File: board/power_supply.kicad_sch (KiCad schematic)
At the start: 51 parts, among them J1 USB, J2 LiPo, J3 On/Off, J5 Temp, Q10 SI2302, Q8 SI2302, U1 LGS4056HEP, U11 FM2113, U2 TLV61048, U3 RT9069, U4 JW5026

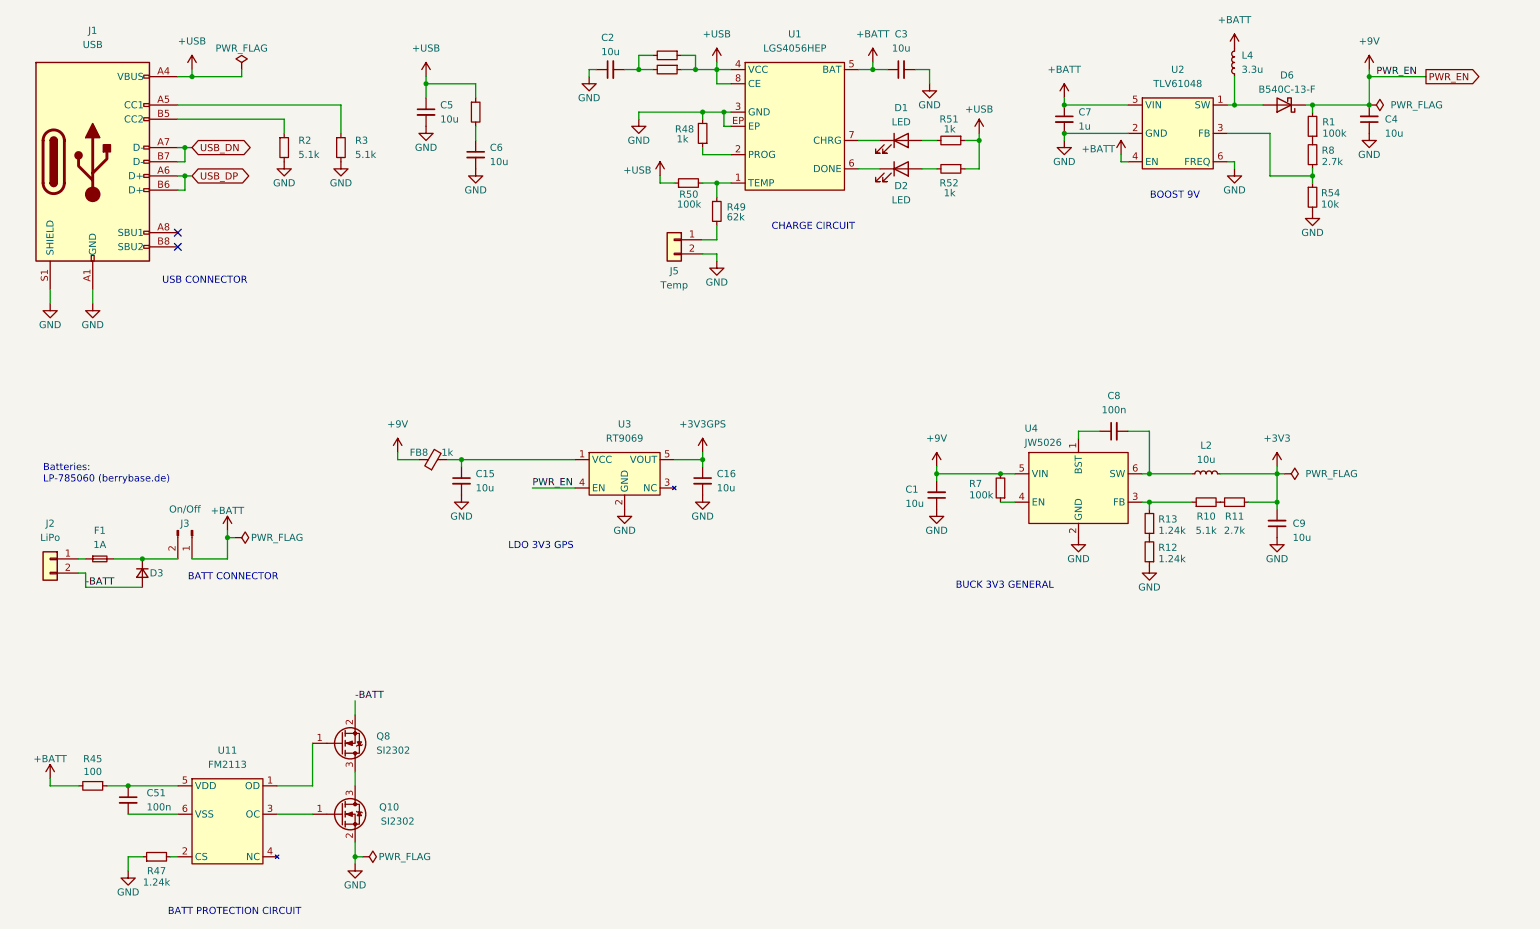
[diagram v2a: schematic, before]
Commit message: Fix errors in schematic for new board design
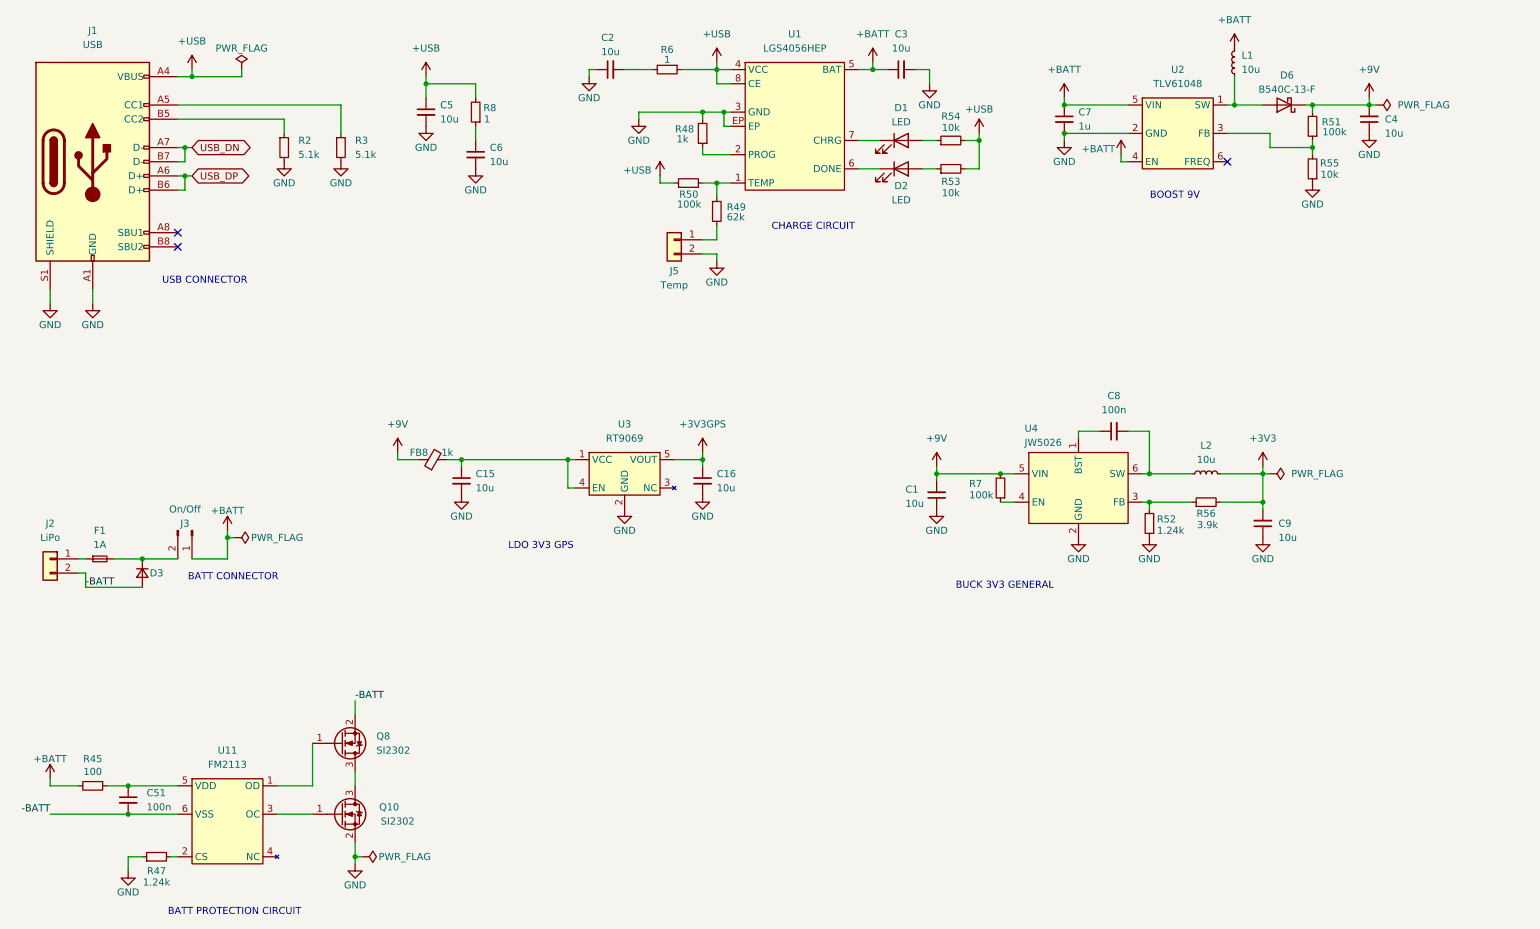
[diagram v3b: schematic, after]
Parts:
- removed L4: 3.3u, symbol Device:L_Small
- removed R1: 100k, Resistor_SMD:R_0603_1608Metric, symbol Device:R_Small
- removed R10: 5.1k, Resistor_SMD:R_0603_1608Metric, symbol Device:R_Small
- removed R11: 2.7k, Resistor_SMD:R_0603_1608Metric, symbol Device:R_Small
- removed R12, R13: 1.24k, Resistor_SMD:R_0603_1608Metric, symbol Device:R_Small
- removed R4, R5: 2, Resistor_SMD:R_0603_1608Metric, symbol Device:R_Small
- added L1: 10u, Inductor_SMD:L_6.3x6.3_H3, symbol Device:L_Small
- added R53, R55: 10k, Resistor_SMD:R_0603_1608Metric, symbol Device:R_Small
- added R56: 3.9k, Resistor_SMD:R_0603_1608Metric, symbol Device:R_Small
- C1, C15, C16, C2, C3, C4, C5, C6, C9: JLC_PN C19702 -> C962136; JLC_Price1 0.062 -> (none); JLC_Price10 0.0052 -> (none); JLC_Price100 0.0031 -> (none); JLC_Price1000 0.0029 -> (none); MPN CL10A106KP8NNNC -> CL10A106KO8NQNC
- D2: JLC_PN (none) -> C12624; JLC_Price1000 0.0036 -> (none)
- L2: footprint (none) -> Inductor_SMD:L_6.3x6.3_H3; JLC_PN (none) -> C168076
- Q10, Q8: JLC_PN (none) -> C2891732
- R49: JLC_PN (none) -> C23221
- R50, R7: JLC_PN (none) -> C25803
- R51: value 1k -> 100k; JLC_PN C21190 -> C25803; JLC_Price10 0.0005 -> (none); MPN 0603WAF1001T5E -> 0603WAF1003T5E; kicost:JLC:pricing 1: USD 0.0005; 200: USD 0.0004 -> (none)
- R52: value 1k -> 1.24k; JLC_BasicPart yes -> no; JLC_PN C21190 -> C25956; JLC_Price10 0.0005 -> (none); MPN 0603WAF1001T5E -> 0603WAF1241T5E; Manufacturer UNI-ROYAL(Uniroyal Elec) -> UNI-ROYAL(Uniroyal Elec); PCBA yes -> (none); kicost:JLC:pricing 1: USD 0.0005; 200: USD 0.0004 -> (none)
- R6: value 2 -> 1; JLC_BasicPart yes -> (none); JLC_PN C22977 -> C22936; JLC_Price10 0.0012 -> (none); MPN 0603WAF200KT5E -> 0603WAF100KT5E; PCBA yes -> (none); kicost:JLC:pricing 1: USD 0.0014; 200: USD 0.0011; 1000: USD 0.0009 -> (none)
- R8: value 2.7k -> 1; JLC_BasicPart yes -> (none); JLC_PN C13167 -> C22936; MPN 0603WAF2701T5E -> 0603WAF100KT5E
- U1: JLC_PN (none) -> C5123970; MPN (none) -> LGS4056HEP; Manufacturer (none) -> Legend-Si
- U2: JLC_PN (none) -> C2861467; MPN (none) -> TLV61048DBVR; Manufacturer (none) -> Texas Instruments
- U4: JLC_PN (none) -> C185109; MPN (none) -> JW5026; Manufacturer (none) -> JoulWatt Tech
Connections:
- net +3V3: now also R56.2
- net +9V: now also R51.2; no longer U3.4 (EN)
- net +BATT: now also L1.2
- net +USB: now also R54.2, R8.2, R53.2; no longer R51.1, R52.1
- net -BATT: now also C51.2, U11.6 (VSS)
- net GND: now also R52.1, R55.1; no longer R54.2, U2.6 (FREQ)
- net at C15.1, FB8.2, U3.1 (VCC): now also U3.4 (EN)
- net at C6.1: now also R8.1
- net at D1.2 (A): now also R54.1; no longer R51.2
- net at D6.2 (A), U2.1 (SW): now also L1.1
- net at D2.2 (A): now also R53.1; no longer R52.2
- net at U4.3 (FB): now also R52.2, R56.1
- new net: R51.1, R55.2, U2.3 (FB)
- no-connect marks 2 -> 3
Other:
- note removed: "Batteries: LP-785060 (berrybase.de)"
- moved on the sheet: C9

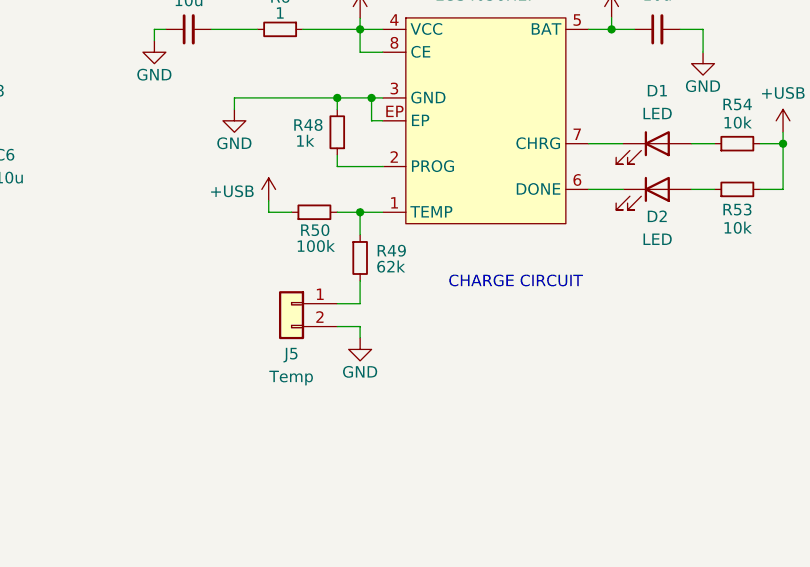
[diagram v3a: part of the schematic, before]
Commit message: Schematic updates
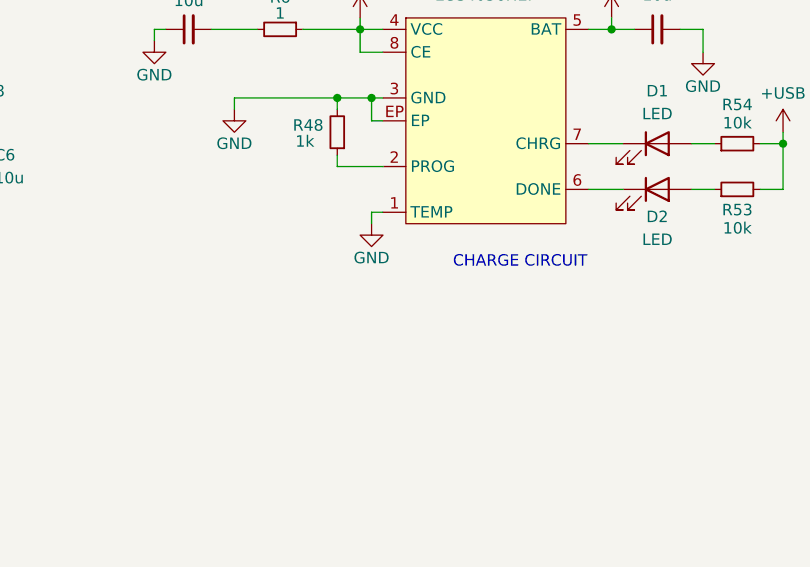
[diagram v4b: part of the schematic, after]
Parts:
- removed J5: Temp, Connector_JST:JST_PH_S2B-PH-K_1x02_P2.00mm_Horizontal, symbol Connector_Generic:Conn_01x02
- removed R49: 62k, Resistor_SMD:R_0603_1608Metric, symbol Device:R_Small
- removed R50: 100k, Resistor_SMD:R_0603_1608Metric, symbol Device:R_Small
- J2: JLC_PN C173752 -> C843326; MPN S2B-PH-K-S(LF)(SN) -> X2510WR-02-N0SN; Manufacturer JST -> XKB Connection
- J3: footprint OpenBikeSensor:Connector_1x02_Switch -> Connector_JST:JST_XH_S2B-XH-A_1x02_P2.50mm_Horizontal; JLC_PN (none) -> C157931; MPN (none) -> S2B-XH-A(LF)(SN); Manufacturer (none) -> JST
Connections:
- net GND: now also U1.1 (TEMP)

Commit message: Update PCB layout
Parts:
- J2: footprint Connector_JST:JST_PH_S2B-PH-K_1x02_P2.00mm_Horizontal -> OBSPro:PSS-254-2W
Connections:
- net GND: now also U1.9 (EP); no longer U1.EP
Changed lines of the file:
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@@
 		(pin "8"
 		)
-		(pin "EP"
+		(pin "9"
 		)
 		(instances
@@
 			)
 		)
-		(property "Footprint" "Connector_JST:JST_PH_S2B-PH-K_1x02_P2.00mm_Horizontal"
+		(property "Footprint" "OBSPro:PSS-254-2W"
 			(at 25.4 113.03 0)
 			(effects

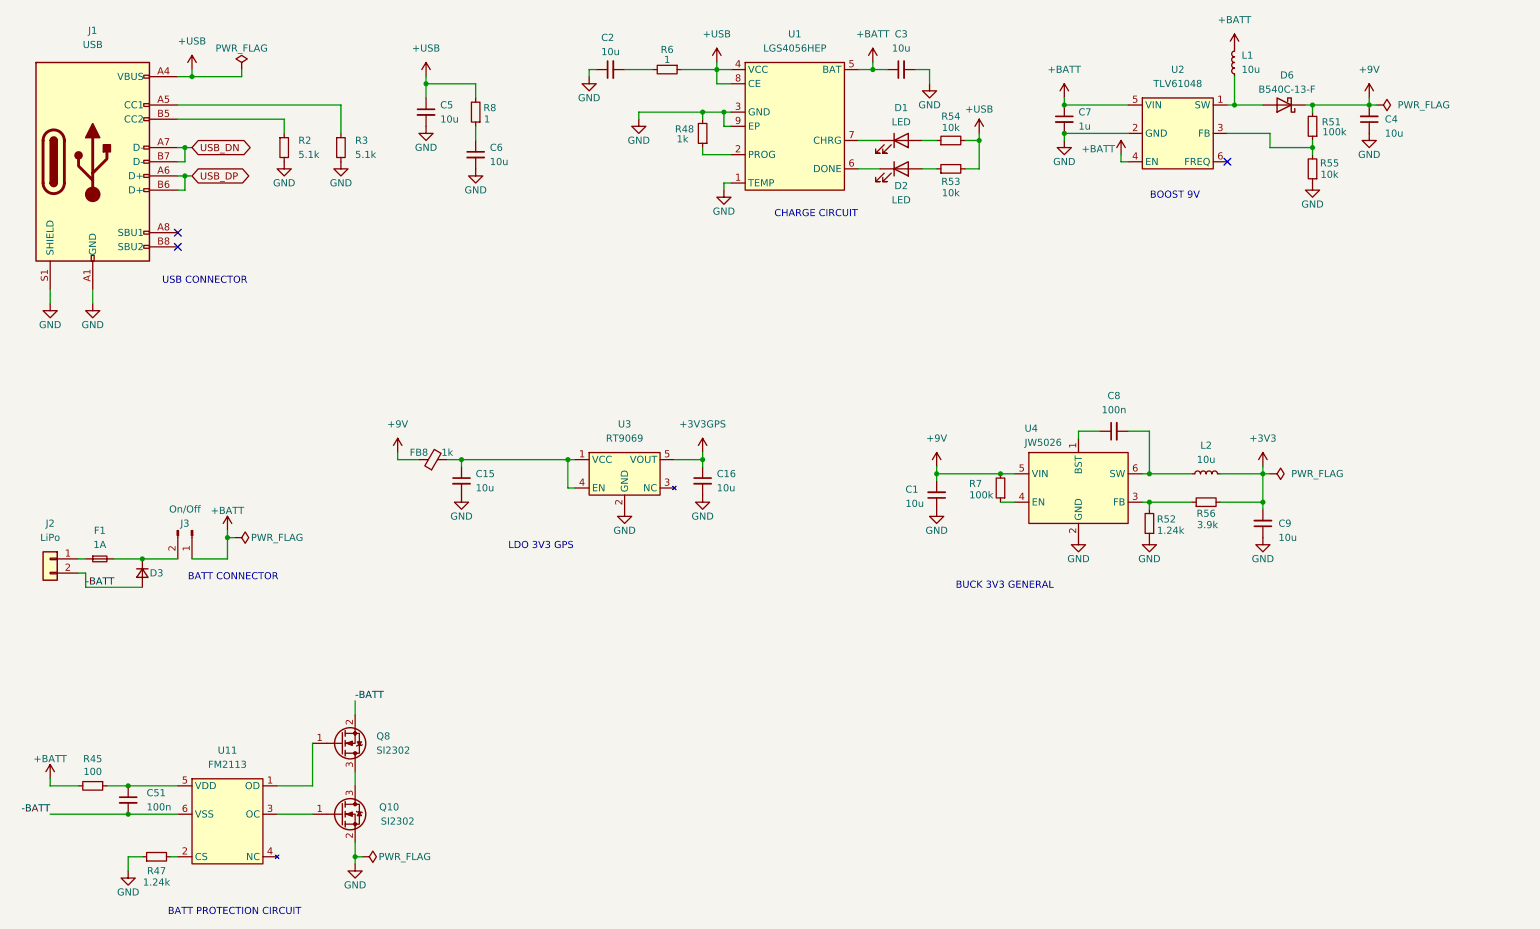
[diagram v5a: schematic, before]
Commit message: Update schematic and PCB layout
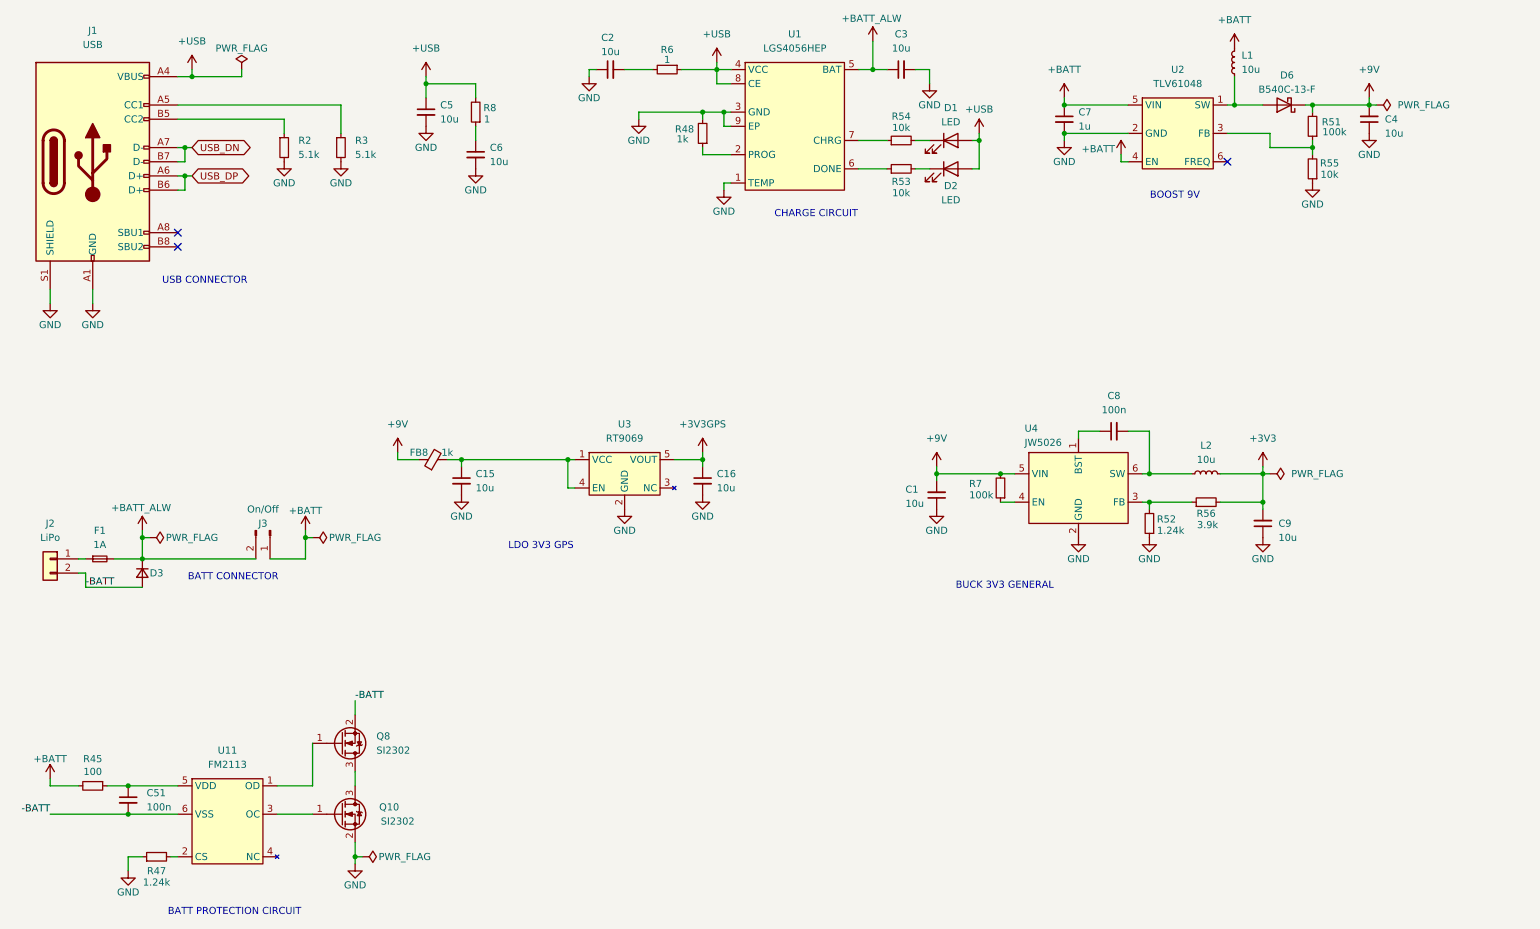
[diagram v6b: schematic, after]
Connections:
- net +BATT: no longer C3.1, U1.5 (BAT)
- net +USB: now also D1.2 (A), D2.2 (A); no longer R53.2, R54.2
- net at R53.1: now also U1.6 (DONE); no longer D2.2 (A)
- net at D2.1 (K): now also R53.2; no longer U1.6 (DONE)
- net at U1.7 (CHRG): now also R54.1; no longer D1.1 (K)
- net +BATT_ALW: now reaches D3.1 (K), F1.2, J3.2 (Pin_2)
- net +BATT_ALW: now also C3.1, U1.5 (BAT)
- new net: D1.1 (K), R54.2
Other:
- moved on the sheet: D1, D2, J3, R53, R54

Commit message: Update schematic and PCB layout
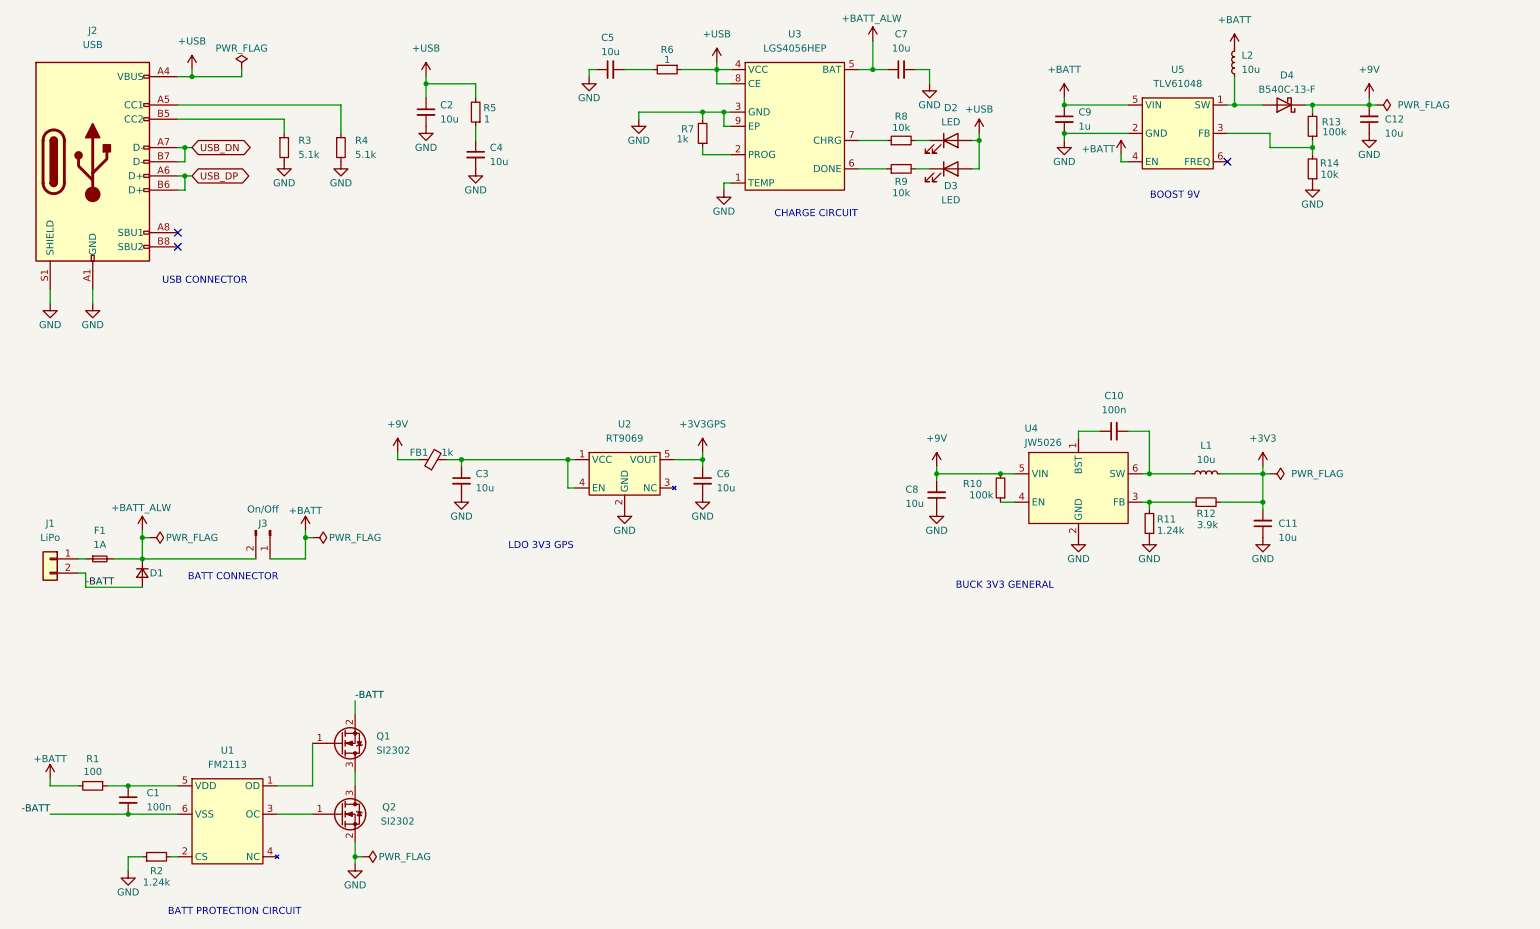
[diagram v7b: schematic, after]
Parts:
- renumbered C51 to C1, C8 to C10, C9 to C11, C4 to C12, C5 to C2, C15 to C3, C6 to C4, C2 to C5, C16 to C6, C3 to C7, C1 to C8, C7 to C9, D3 to D1, D1 to D2, D2 to D3, D6 to D4, FB8 to FB1, J2 to J1, J1 to J2, L2 to L1, L1 to L2, Q8 to Q1, Q10 to Q2, R45 to R1, R7 to R10, R52 to R11, R56 to R12, R51 to R13, R55 to R14, R47 to R2, R2 to R3, R3 to R4, R8 to R5, R48 to R7, R54 to R8, R53 to R9, U11 to U1, U3 to U2, U1 to U3, U2 to U5
